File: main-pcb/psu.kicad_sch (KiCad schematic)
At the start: 110 parts, among them J1 CONN_01X03, J2 CORTEX_DEBUG_ETM, SW1 SWITCH, SW2 SWITCH, U11 LTC3374-QFN, U19 INA230, U2 STM32L431-QFN48, U3 INA230, U4 INA230, U5 INA230, U6 INA230, U7 INA230, U8 INA230

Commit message: Initial design mostly done aside from USB connector, review, test points
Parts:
- added C15: 0.47 uF, azonenberg_pcb:EIA_0402_CAP_NOSILK, symbol device:C
- added C16: 22 uF, symbol device:C
- added C176: 0.47 uF, symbol device:C
- added C177: DNP, symbol device:C
- added JP1: JUMPER_PWROUT, symbol power-azonenberg:JUMPER_PWROUT
- added JP2, JP3, JP4: Jumper, symbol device:Jumper
- added R92: 10K, symbol device:R
- added R93: 25 mR, symbol passive-azonenberg:R_PWR
- added U10: NCP45525IMNTWG-H, symbol power-azonenberg:NCP45525
- added U9: INA230, azonenberg_pcb:QFN_16_0.5MM_3x3MM, symbol special-azonenberg:INA230
- R21, R22, R23, R76, R80, R9, R91: symbol device:R -> passive-azonenberg:R_PWR
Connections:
- net 1V0_SHIN: now also L7.1; no longer L7.2
- net 1V0_SW: now also L7.2; no longer L7.1
- net 1V2: now also JP4.1
- net 1V2_SHIN: now also L6.1; no longer L6.2
- net 1V8: now also JP3.1
- net 1V8_SHIN: now also L5.1; no longer L5.2
- net 2V5: now also JP2.1
- net 2V5_SHIN: now also L2.1; no longer L2.2
- net 3V3: now also C176.1, JP1.1, U10.3 (VCC)
- net 3V3_SB: now also C15.1, U9.1 (A1), U9.9 (Vs+)
- net 3V3_SB_SHIN: now also L3.1; no longer L3.2
- net 3V3_SHIN: now also L1.1; no longer L1.2
- net 3V3_SW: now also L1.2; no longer L1.1
- net DUT_VDD_EN: now also R92.1, U10.2 (EN)
- net GND: now also C15.2, C16.2, C176.2, C177.2, R92.2, U10.4 (GND), U9.10 (GND), U9.PAD (GND)
- net INA_ALERT: now also U9.3 (Alert)
- net SUPER_I2C_SCL: now also U9.2 (A0), U9.5 (SCL)
- net SUPER_I2C_SDA: now also U9.4 (SDA)
- net VBUS: now also R9.2; no longer R9.1
- net VBUS_SHOUT: now also R9.1; no longer R9.2
- net at U11.9 (SW3): now also L2.2; no longer L2.1
- net at U11.22 (SW5): now also L5.2; no longer L5.1
- net at U11.23 (SW6): now also L6.2; no longer L6.1
- net at U11.10 (SW4): now also L3.2; no longer L3.1
- new net: C177.1, U10.6 (SR)
- new net DUT_VDD: R93.1, U9.11 (Vbus), U9.12 (Vin-)
- new net DUT_VDD_RAW: JP1.2, JP2.2, JP3.2, JP4.2, U10.1 (VIN), U10.PAD (VIN)
- new net DUT_VDD_SHIN: C16.1, R93.2, U10.5 (BLEED), U10.7 (VOUT), U10.8 (VOUT), U9.13 (Vin+)
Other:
- note added: "DUT_VDD current monitor: 0x8e"
- moved on the sheet: C10, C11, C12, C13, C14, C175, C9, D1, D2, D3, L1, L2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

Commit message: Finished initial schematic pass, ready for review
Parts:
- added TP15: CONN_01X07, symbol conn:CONN_01X07
- added TP16: U.FL, azonenberg_pcb:CONN_U.FL_TE_1909763-1, symbol conn:CONN_COAXIAL
- JP1: value JUMPER_PWROUT -> Jumper
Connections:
- net DUT_VCCIO_EN: now also TP15.3 (P3)
- net DUT_VDD: now also TP16.1 (In)
- net DUT_VDD_EN: now also TP15.2 (P2)
- net GND: now also TP15.7 (P7), TP16.2 (Ext)
- net INA_ALERT: now also TP15.4 (P4)
- net LTC_PGOOD_ALL: now also TP15.1 (P1)
- net SUPER_I2C_SCL: now also TP15.6 (P6)
- net SUPER_I2C_SDA: now also TP15.5 (P5)

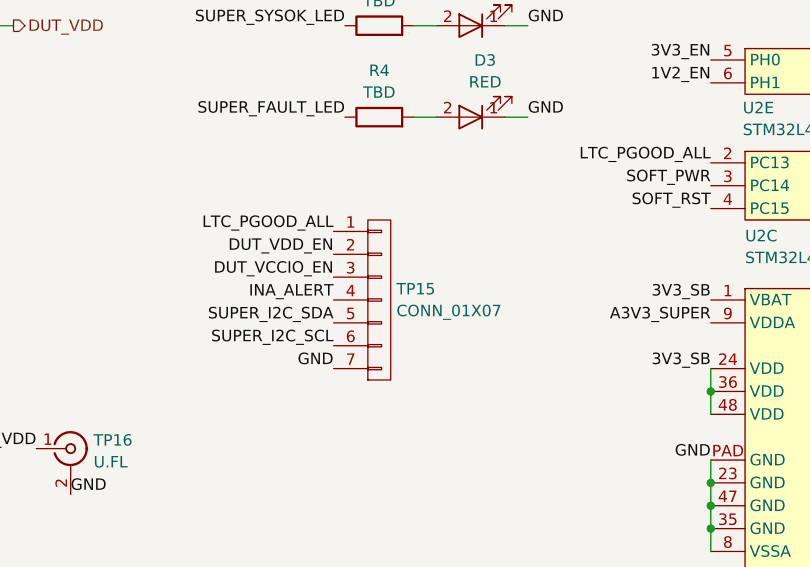
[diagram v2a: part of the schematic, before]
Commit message: More schematic tweaks and test points
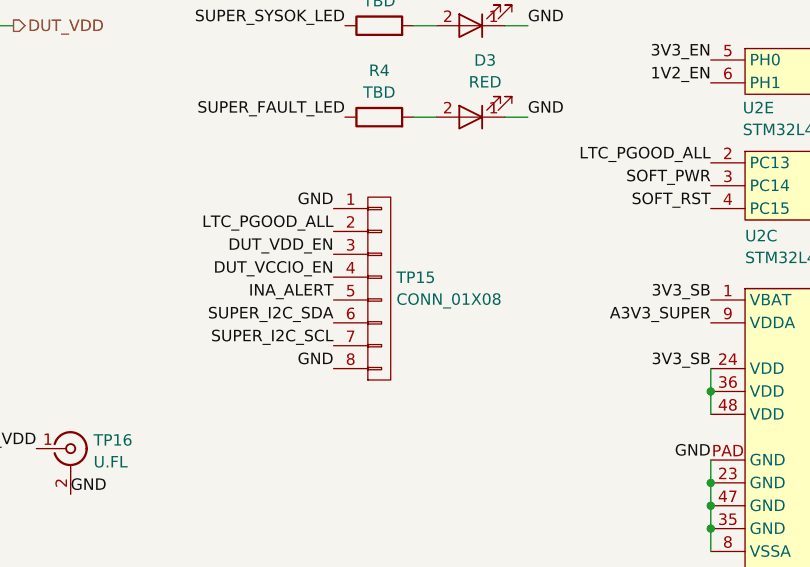
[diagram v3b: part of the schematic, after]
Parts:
- removed TP15: CONN_01X07, symbol conn:CONN_01X07
- added TP15: CONN_01X08, azonenberg_pcb:CONN_HEADER_2.54MM_1x8, symbol conn:CONN_01X08
- C101, C167, C170, C172, C173, C176, C177, C94, C97, C98: footprint (none) -> azonenberg_pcb:EIA_0402_CAP_NOSILK
- D1, D2, D3: footprint (none) -> azonenberg_pcb:EIA_0402_LED
- JP1, JP2, JP3, JP4: footprint (none) -> azonenberg_pcb:CONN_HEADER_2.54MM_1x2
- L1, L2, L3, L5, L6, L7: footprint (none) -> azonenberg_pcb:EIA_1210_CAP_NOSILK
- R10, R13, R14, R15, R18, R19, R20, R21, R22, R23, R75, R76, R77, R78, R79, R80, R82, R83, R84, R85, R86, R87, R88, R89, R9, R90, R91, R92, R93: footprint (none) -> azonenberg_pcb:EIA_0402_RES_NOSILK
- U10: footprint (none) -> azonenberg_pcb:DFN_8_0.5MM_2x2MM
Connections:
- net DUT_VCCIO_EN: now also TP15.4 (P4)
- net DUT_VDD_EN: now also TP15.3 (P3)
- net GND: now also TP15.1 (P1), TP15.8 (P8)
- net INA_ALERT: now also TP15.5 (P5)
- net LTC_PGOOD_ALL: now also TP15.2 (P2)
- net SUPER_I2C_SCL: now also TP15.7 (P7)
- net SUPER_I2C_SDA: now also TP15.6 (P6)

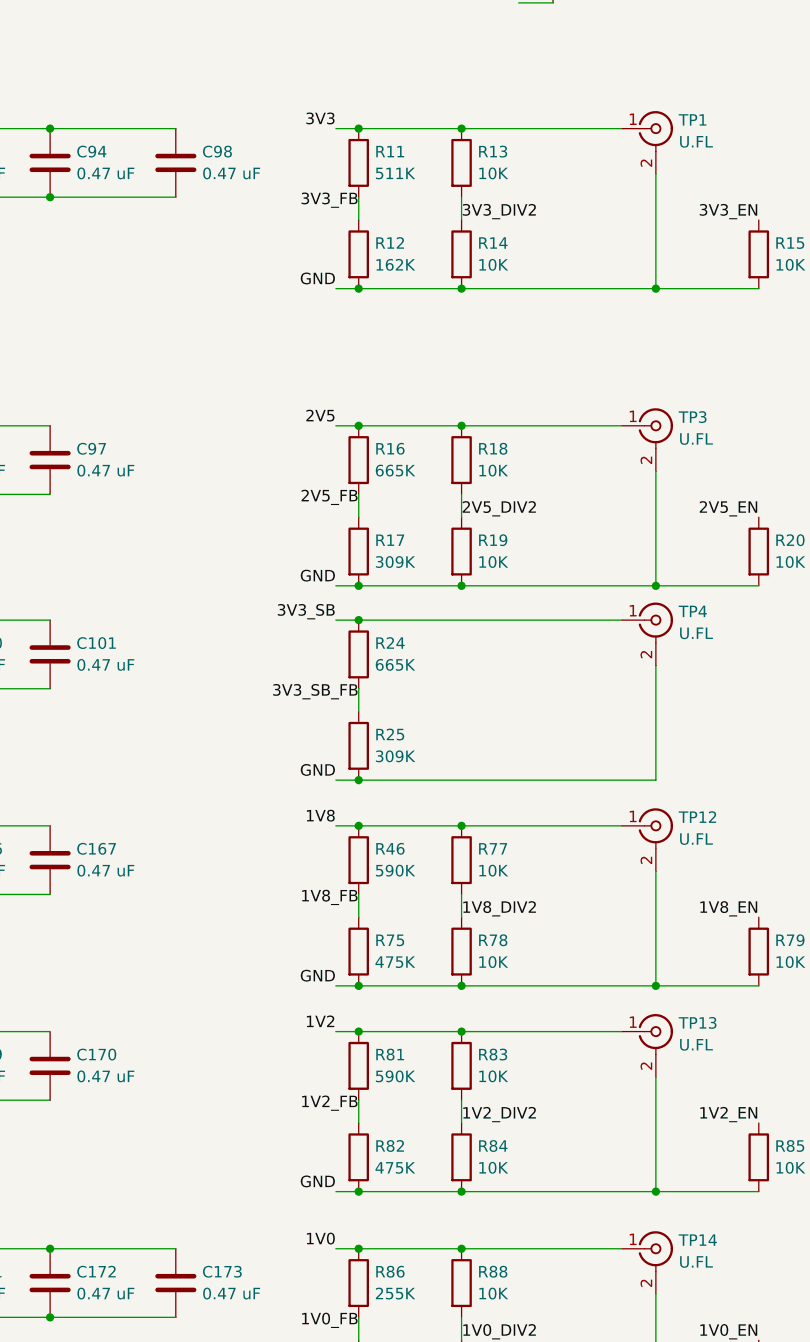
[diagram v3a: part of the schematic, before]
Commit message: Added some RGB LEDs, changed a few voltage dividers to match what was in stock. Time for next round of review.
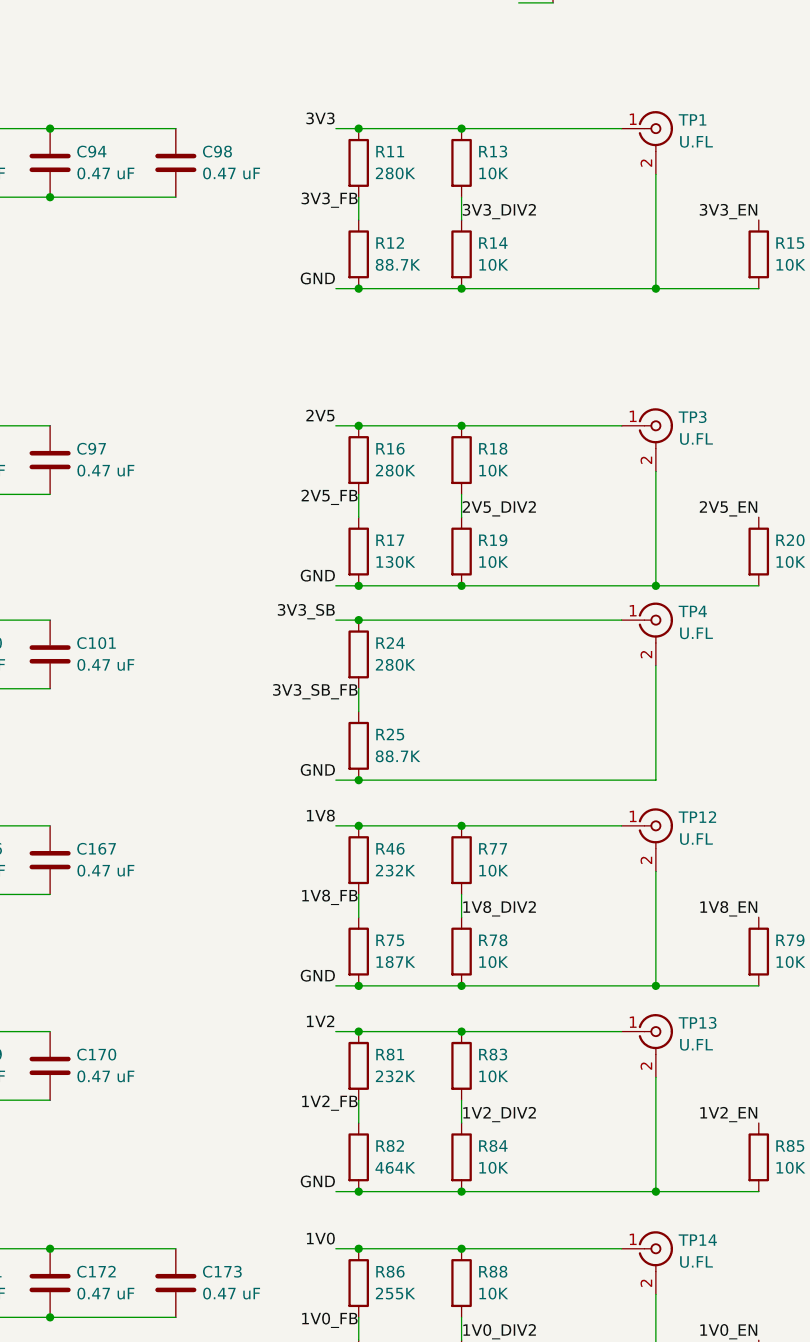
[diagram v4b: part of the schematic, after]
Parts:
- C100, C135, C166, C169, C95: footprint (none) -> azonenberg_pcb:EIA_1206_CAP_NOSILK
- C16, C171, C174, C91, C92, C93, C96, C99: footprint (none) -> azonenberg_pcb:EIA_1210_CAP_NOSILK
- C168: footprint (none) -> azonenberg_pcb:EIA_0805_CAP_NOSILK
- R11: value 511K -> 280K; footprint (none) -> azonenberg_pcb:EIA_0402_RES_NOSILK
- R12: value 162K -> 88.7K; footprint (none) -> azonenberg_pcb:EIA_0402_RES_NOSILK
- R16, R24: value 665K -> 280K; footprint (none) -> azonenberg_pcb:EIA_0402_RES_NOSILK
- R17: value 309K -> 130K; footprint (none) -> azonenberg_pcb:EIA_0402_RES_NOSILK
- R25: value 309K -> 88.7K; footprint (none) -> azonenberg_pcb:EIA_0402_RES_NOSILK
- R46, R81: value 590K -> 232K; footprint (none) -> azonenberg_pcb:EIA_0402_RES_NOSILK
- R75: value 475K -> 187K
- R82: value 475K -> 464K
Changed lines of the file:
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@@
 	(title_block
 		(title "DUMPTRUCK flash dumper")
-		(date "2024-10-16")
+		(date "2024-10-17")
 		(rev "0.1")
 		(company "Antikernel Labs")
@@
 			)
 		)
-		(property "Value" "309K"
+		(property "Value" "130K"
 			(at 171.958 88.8421 0)
 			(effects
@@
 			)
 		)
-		(property "Footprint" ""
+		(property "Footprint" "azonenberg_pcb:EIA_0402_RES_NOSILK"
 			(at 168.402 87.63 90)
 			(effects
@@
 			)
 		)
-		(property "Value" "309K"
+		(property "Value" "88.7K"
 			(at 171.958 110.4321 0)
 			(effects
@@
 			)
 		)
-		(property "Footprint" ""
+		(property "Footprint" "azonenberg_pcb:EIA_0402_RES_NOSILK"
 			(at 168.402 109.22 90)
 			(effects
@@
 			)
 		)
-		(property "Value" "590K"
+		(property "Value" "232K"
 			(at 171.958 123.1321 0)
 			(effects
@@
 			)
 		)
-		(property "Footprint" ""
+		(property "Footprint" "azonenberg_pcb:EIA_0402_RES_NOSILK"
 			(at 168.402 121.92 90)
 			(effects
@@
 			)
 		)
-		(property "Footprint" ""
+		(property "Footprint" "azonenberg_pcb:EIA_1210_CAP_NOSILK"
 			(at 124.1552 172.72 0)
 			(effects
@@
 			)
 		)
-		(property "Value" "665K"
+		(property "Value" "280K"
 			(at 171.958 78.6821 0)
 			(effects
@@
 			)
 		)
-		(property "Footprint" ""
+		(property "Footprint" "azonenberg_pcb:EIA_0402_RES_NOSILK"
 			(at 168.402 77.47 90)
 			(effects
@@
 			)
 		)
-		(property "Value" "511K"
+		(property "Value" "280K"
 			(at 171.958 45.6621 0)
 			(effects
@@
 			)
 		)
-		(property "Footprint" ""
+		(property "Footprint" "azonenberg_pcb:EIA_0402_RES_NOSILK"
 			(at 168.402 44.45 90)
 			(effects
@@
 			)
 		)
-		(property "Footprint" ""
+		(property "Footprint" "azonenberg_pcb:EIA_1210_CAP_NOSILK"
 			(at 60.6552 31.75 0)
 			(effects
@@
 			)
 		)
-		(property "Footprint" ""
+		(property "Footprint" "azonenberg_pcb:EIA_1206_CAP_NOSILK"
 			(at 124.1552 102.87 0)
 			(effects
@@
 			)
 		)
-		(property "Footprint" ""
+		(property "Footprint" "azonenberg_pcb:EIA_1210_CAP_NOSILK"
 			(at 46.6852 57.15 0)
 			(effects
@@
 			)
 		)
-		(property "Footprint" ""
+		(property "Footprint" "azonenberg_pcb:EIA_1210_CAP_NOSILK"
 			(at 124.1552 48.26 0)
 			(effects
@@
 			)
 		)
-		(property "Value" "475K"
+		(property "Value" "464K"
 			(at 171.958 156.1521 0)
 			(effects
@@
 			)
 		)
-		(property "Value" "590K"
+		(property "Value" "232K"
 			(at 171.958 145.9921 0)
 			(effects
@@
 			)
 		)
-		(property "Footprint" ""
+		(property "Footprint" "azonenberg_pcb:EIA_0402_RES_NOSILK"
 			(at 168.402 144.78 90)
 			(effects
@@
 			)
 		)
-		(property "Value" "162K"
+		(property "Value" "88.7K"
 			(at 171.958 55.8221 0)
 			(effects
@@
 			)
 		)
-		(property "Footprint" ""
+		(property "Footprint" "azonenberg_pcb:EIA_0402_RES_NOSILK"
 			(at 168.402 54.61 90)
 			(effects
@@
 			)
 		)
-		(property "Footprint" ""
+		(property "Footprint" "azonenberg_pcb:EIA_1210_CAP_NOSILK"
 			(at 49.2252 111.76 0)
 			(effects
@@
 			)
 		)
-		(property "Footprint" ""
+		(property "Footprint" "azonenberg_pcb:EIA_1210_CAP_NOSILK"
 			(at 124.1552 81.28 0)
 			(effects
@@
 			)
 		)
-		(property "Footprint" ""
+		(property "Footprint" "azonenberg_pcb:EIA_1206_CAP_NOSILK"
 			(at 49.2252 134.62 0)
 			(effects
@@
 			)
 		)
-		(property "Footprint" ""
+		(property "Footprint" "azonenberg_pcb:EIA_1210_CAP_NOSILK"
 			(at 89.8652 213.36 0)
 			(effects
@@
 			)
 		)
-		(property "Footprint" ""
+		(property "Footprint" "azonenberg_pcb:EIA_1206_CAP_NOSILK"
 			(at 124.1552 125.73 0)
 			(effects
@@
 			)
 		)
-		(property "Value" "665K"
+		(property "Value" "280K"
 			(at 171.958 100.2721 0)
 			(effects
@@
 			)
 		)
-		(property "Footprint" ""
+		(property "Footprint" "azonenberg_pcb:EIA_0402_RES_NOSILK"
 			(at 168.402 99.06 90)
 			(effects
@@
 			)
 		)
-		(property "Value" "475K"
+		(property "Value" "187K"
 			(at 171.958 133.2921 0)
 			(effects
@@
 			)
 		)
-		(property "Footprint" ""
+		(property "Footprint" "azonenberg_pcb:EIA_1210_CAP_NOSILK"
 			(at 46.6852 181.61 0)
 			(effects
@@
 			)
 		)
-		(property "Footprint" ""
+		(property "Footprint" "azonenberg_pcb:EIA_0805_CAP_NOSILK"
 			(at 49.2252 157.48 0)
 			(effects
@@
 			)
 		)
-		(property "Footprint" ""
+		(property "Footprint" "azonenberg_pcb:EIA_1206_CAP_NOSILK"
 			(at 49.2252 90.17 0)
 			(effects
@@
 			)
 		)
-		(property "Footprint" ""
+		(property "Footprint" "azonenberg_pcb:EIA_1206_CAP_NOSILK"
 			(at 124.1552 148.59 0)
 			(effects

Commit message: Finished schematic review
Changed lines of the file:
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@@
 	(wire
 		(pts
+			(xy 59.69 15.24) (xy 59.69 24.13)
+		)
+		(stroke
+			(width 0)
+			(type default)
+		)
+	)
+	(wire
+		(pts
 			(xy 170.18 81.28) (xy 170.18 83.82)
 		)
@@
 		)
 	)
-	(label "VBUS_SHOUT"
-		(at 53.34 24.13 0)
-		(fields_autoplaced yes)
-		(effects
-			(font
-				(size 1.27 1.27)
-			)
-			(justify left bottom)
-		)
-	)
 	(label "SUPER_FAULT_LED"
 		(at 255.27 93.98 180)
@@
 		(fields_autoplaced yes)
 		(effects
+			(font
+				(size 1.27 1.27)
+			)
+			(justify right)
+		)
+	)
+	(hierarchical_label "VBUS_SHOUT"
+		(shape output)
+		(at 59.69 15.24 180)
+		(fields_autoplaced yes)
+		(effects

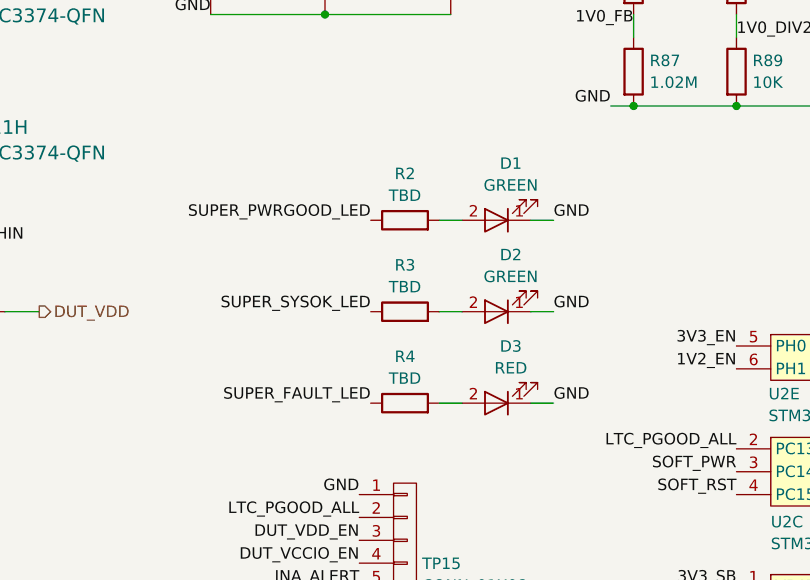
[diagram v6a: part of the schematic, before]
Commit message: Continued layout mostly of DUT connectors
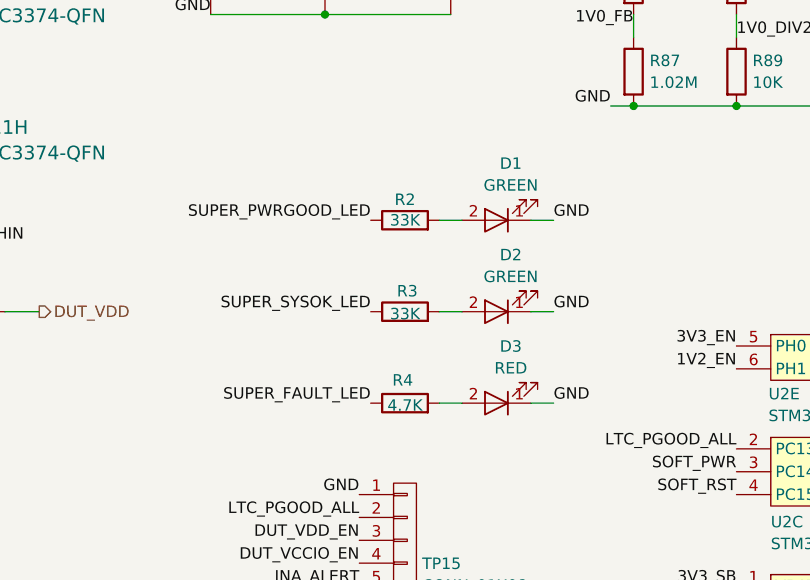
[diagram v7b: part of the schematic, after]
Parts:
- R2, R3: value TBD -> 33K
- R4: value TBD -> 4.7K
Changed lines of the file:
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@@
 	(title_block
 		(title "DUMPTRUCK flash dumper")
-		(date "2024-10-18")
+		(date "2024-10-19")
 		(rev "0.1")
 		(company "Antikernel Labs")
@@
 		(on_board yes)
 		(dnp no)
-		(fields_autoplaced yes)
 		(property "Reference" "R4"
-			(at 144.78 210.7395 90)
+			(at 144.526 213.36 90)
 			(effects
 				(font
@@
 			)
 		)
-		(property "Value" "TBD"
-			(at 144.78 213.1638 90)
+		(property "Value" "4.7K"
+			(at 144.78 216.154 90)
 			(effects
 				(font
@@
 		(on_board yes)
 		(dnp no)
-		(fields_autoplaced yes)
 		(property "Reference" "R3"
-			(at 144.78 200.5795 90)
+			(at 145.034 203.454 90)
 			(effects
 				(font
@@
 			)
 		)
-		(property "Value" "TBD"
-			(at 144.78 203.0038 90)
+		(property "Value" "33K"
+			(at 144.78 205.994 90)
 			(effects
 				(font
@@
 		(on_board yes)
 		(dnp no)
-		(fields_autoplaced yes)
 		(property "Reference" "R2"
-			(at 144.78 190.4195 90)
+			(at 144.78 193.294 90)
 			(effects
 				(font
@@
 			)
 		)
-		(property "Value" "TBD"
-			(at 144.78 192.8438 90)
+		(property "Value" "33K"
+			(at 144.78 195.58 90)
 			(effects
 				(font
